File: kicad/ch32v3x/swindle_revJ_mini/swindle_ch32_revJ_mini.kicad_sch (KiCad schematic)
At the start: 16 parts, among them J2_DFU1 con2, U1 CH32V303RCT6, Y1 8Mhz

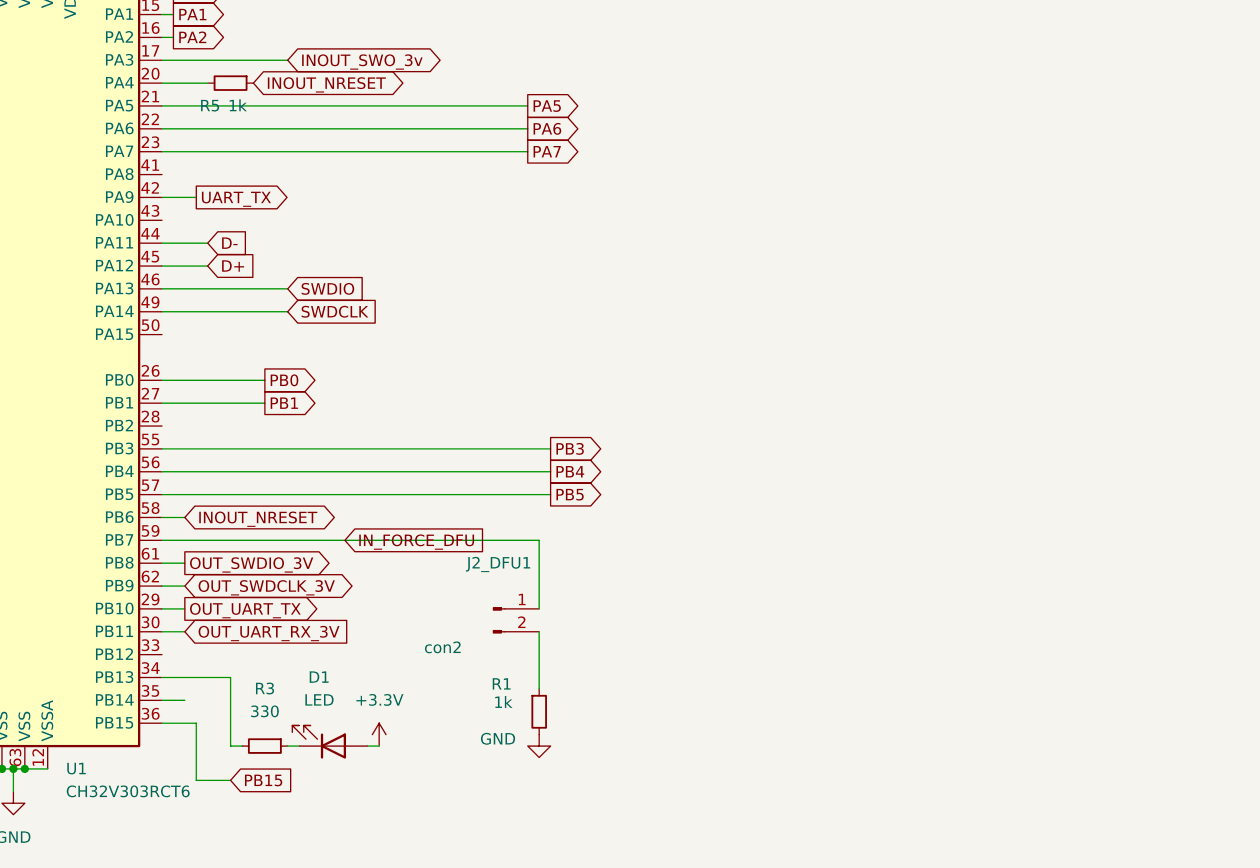
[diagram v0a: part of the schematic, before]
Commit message: add a WS2812b to the mini version, mini version for CH32,GD32 and RP2xxx
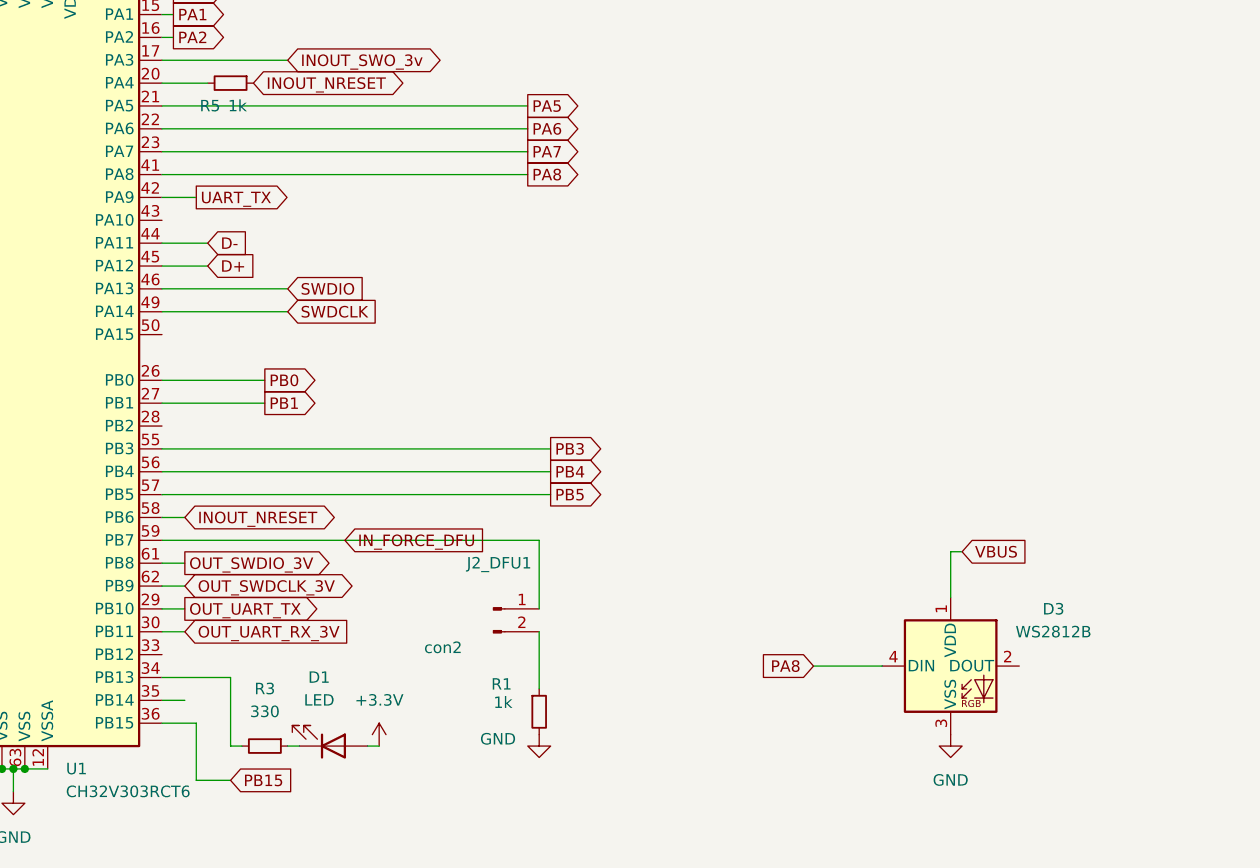
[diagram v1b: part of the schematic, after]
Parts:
- added D3: WS2812B, LED_SMD:LED_WS2812B_PLCC4_5.0x5.0mm_P3.2mm, symbol LED:WS2812B
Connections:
- net GND: now also D3.3 (VSS)
- net PA8: now reaches U1.41 (PA8)
- net PA8: now also D3.4 (DIN)
- new net VBUS: D3.1 (VDD)
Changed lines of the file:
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@@
 	(wire
 		(pts
+			(xy 175.26 129.54) (xy 173.99 129.54)
+		)
+		(stroke
+			(width 0)
+			(type default)
+		)
+	)
+	(wire
+		(pts
 			(xy 38.1 58.42) (xy 38.1 59.69)
 		)
@@
 	(wire
 		(pts
+			(xy 86.36 87.63) (xy 127 87.63)
+		)
+		(stroke
+			(width 0)
+			(type default)
+		)
+	)
+	(wire
+		(pts
 			(xy 86.36 95.25) (xy 91.44 95.25)
 		)
@@
 	(wire
 		(pts
+			(xy 158.75 142.24) (xy 166.37 142.24)
+		)
+		(stroke
+			(width 0)
+			(type default)
+		)
+	)
+	(wire
+		(pts
 			(xy 38.1 43.18) (xy 38.1 44.45)
 		)
@@
 	(wire
 		(pts
+			(xy 173.99 129.54) (xy 173.99 134.62)
+		)
+		(stroke
+			(width 0)
+			(type default)
+		)
+	)
+	(wire
+		(pts
 			(xy 86.36 102.87) (xy 100.33 102.87)
 		)
@@
 		)
 	)
+	(global_label "PA8"
+		(shape input)
+		(at 158.75 142.24 180)
+		(fields_autoplaced yes)
+		(effects
+			(font
+				(size 1.27 1.27)
+			)
+			(justify right)
+		)
+		(property "Intersheetrefs" "${INTERSHEET_REFS}"
+			(at 152.1967 142.24 0)
+			(effects
+				(font
+					(size 1.27 1.27)
+				)
+				(justify right)
+				(hide yes)
+			)
+		)
+	)
 	(global_label "PB1"
 		(shape output)
@@
 		)
 	)
+	(global_label "PA8"
+		(shape output)
+		(at 127 87.63 0)
+		(fields_autoplaced yes)
+		(effects
+			(font
+				(size 1.27 1.27)
+			)
+			(justify left)
+		)
+		(property "Intersheetrefs" "${INTERSHEET_REFS}"
+			(at 133.5533 87.63 0)
+			(effects
+				(font
+					(size 1.27 1.27)
+				)
+				(justify left)
+				(hide yes)
+			)
+		)
+	)
 	(global_label "OUT_UART_TX"
 		(shape output)
@@
 		)
 	)
+	(global_label "VBUS"
+		(shape input)
+		(at 175.26 129.54 0)
+		(fields_autoplaced yes)
+		(effects
+			(font
+				(size 1.27 1.27)
+			)
+			(justify left)
+		)
+		(property "Intersheetrefs" "${INTERSHEET_REFS}"
+			(at 183.1438 129.54 0)
+			(effects
+				(font
+					(size 1.27 1.27)
+				)
+				(justify left)
+				(hide yes)
+			)
+		)
+	)
 	(global_label "PA6"
 		(shape output)
@@
 	)
 	(symbol
+		(lib_id "LED:WS2812B")
+		(at 173.99 142.24 0)
+		(unit 1)
+		(exclude_from_sim no)
+		(in_bom yes)
+		(on_board yes)
+		(dnp no)
+		(fields_autoplaced yes)
+		(property "Reference" "D3"
+			(at 185.42 135.9214 0)
+			(effects
+				(font
+					(size 1.27 1.27)
+				)
+			)
+		)
+		(property "Value" "WS2812B"
+			(at 185.42 138.4614 0)
+			(effects
+				(font
+					(size 1.27 1.27)
+				)
+			)
+		)
+		(property "Footprint" "LED_SMD:LED_WS2812B_PLCC4_5.0x5.0mm_P3.2mm"
+			(at 175.26 149.86 0)
+			(effects
+				(font
+					(size 1.27 1.27)
+				)
+				(justify left top)
+				(hide yes)
+			)
+		)
+		(property "Datasheet" "https://cdn-shop.adafruit.com/datasheets/WS2812B.pdf"
+			(at 176.53 151.765 0)
+			(effects
+				(font
+					(size 1.27 1.27)
+				)
+				(justify left top)
+				(hide yes)
+			)
+		)
+		(property "Description" "RGB LED with integrated controller"
+			(at 173.99 142.24 0)
+			(effects
+				(font
+					(size 1.27 1.27)
+				)
+				(hide yes)
+			)
+		)
+		(pin "2"
+		)
+		(pin "1"
+		)
+		(pin "4"
+		)
+		(pin "3"
+		)
+		(instances
+			(project "swindle_ch32_revJ_mini"
+				(path "/fbe443d6-6d74-4abc-9dee-16e0160553bc"
+					(reference "D3")
+					(unit 1)
+				)
+			)
+		)
+	)
+	(symbol
 		(lib_id "Device:C_Small")
 		(at 119.38 26.67 0)
@@
 					(unit 1)
 				)
+			)
+		)
+	)
+	(symbol
+		(lib_id "power:GND")
+		(at 173.99 149.86 0)
+		(unit 1)
+		(exclude_from_sim no)
+		(in_bom yes)
+		(on_board yes)
+		(dnp no)
+		(fields_autoplaced yes)
+		(property "Reference" "#PWR037"
+			(at 173.99 156.21 0)
+			(effects
+				(font
+					(size 1.27 1.27)
+				)
+				(hide yes)
+			)
+		)
+		(property "Value" "GND"
+			(at 173.99 154.94 0)
+			(effects
+				(font
+					(size 1.27 1.27)
+				)
+			)
+		)
+		(property "Footprint" ""
+			(at 173.99 149.86 0)
+			(effects
+				(font
+					(size 1.27 1.27)
+				)
+				(hide yes)
+			)
+		)
+		(property "Datasheet" ""
+			(at 173.99 149.86 0)
+			(effects
+				(font
+					(size 1.27 1.27)
+				)
+				(hide yes)
+			)
+		)
+		(property "Description" ""
+			(at 173.99 149.86 0)
+			(effects
+				(font
+					(size 1.27 1.27)
+				)
+				(hide yes)
+			)
+		)
+		(pin "1"
+		)
+		(instances
+			(project "swindle_ch32_revJ_mini"
+				(path "/fbe443d6-6d74-4abc-9dee-16e0160553bc"
+					(reference "#PWR037")
+					(unit 1)
+				)

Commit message: kicad: order to pcbway
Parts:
- added C10: 100n, Resistor_SMD:R_0603_1608Metric, symbol Device:C_Small
- added Q1: DMG2302U, Package_TO_SOT_SMD:SOT-23, symbol Transistor_FET:DMG2302U
- added R8: 330, Resistor_SMD:R_0603_1608Metric, symbol Device:R_Small
- added R9: 1k, Resistor_SMD:R_0603_1608Metric, symbol Device:R_Small
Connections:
- net GND: now also C10.2, Q1.2 (S), R9.2
- net INOUT_NRESET: now also R8.1; no longer U1.58 (PB6)
- net PA8: no longer D3.4 (DIN)
- net PB4: now also D3.4 (DIN)
- net VBUS: now also C10.1
- new net: Q1.3 (D), R8.2
- new net DRIVE_RESET: Q1.1 (G), R9.1, U1.58 (PB6)

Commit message: kicad: rename the mostfet as A2SHB
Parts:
- renumbered Q1 to Q1-A2SHB
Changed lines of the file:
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@@
 		(dnp no)
 		(fields_autoplaced yes)
-		(property "Reference" "Q1"
+		(property "Reference" "Q1-A2SHB"
 			(at 186.69 86.3599 0)
 			(effects
@@
 			(project ""
 				(path "/fbe443d6-6d74-4abc-9dee-16e0160553bc"
-					(reference "Q1")
+					(reference "Q1-A2SHB")
 					(unit 1)
 				)

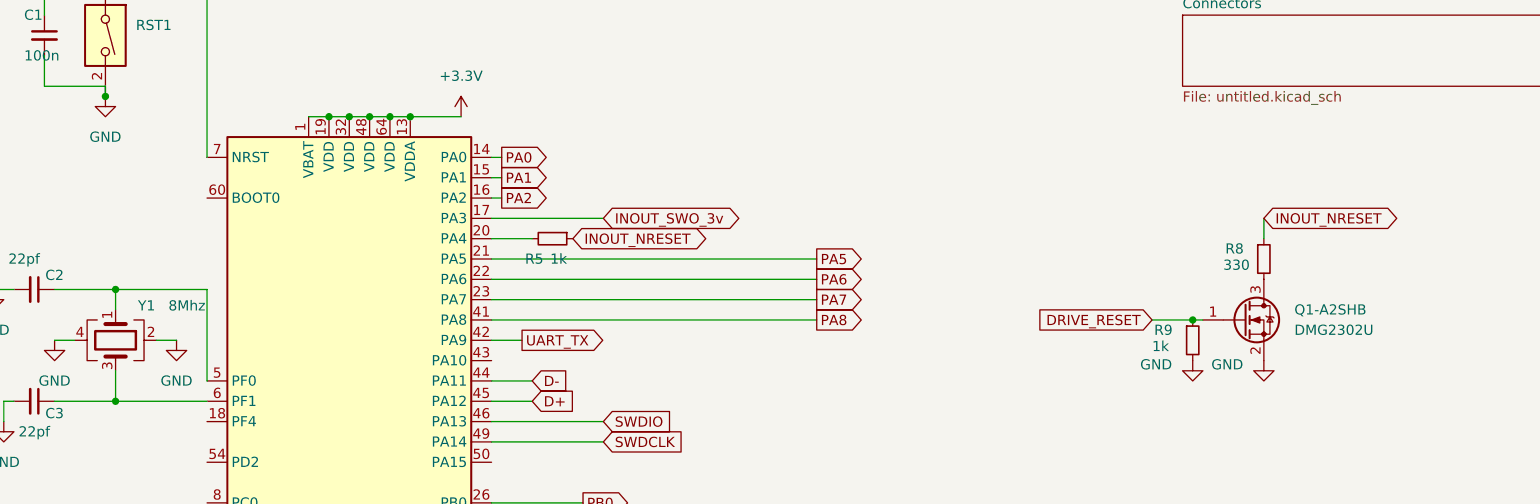
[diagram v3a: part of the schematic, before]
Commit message: kicad/ch32 mini : fix boot0
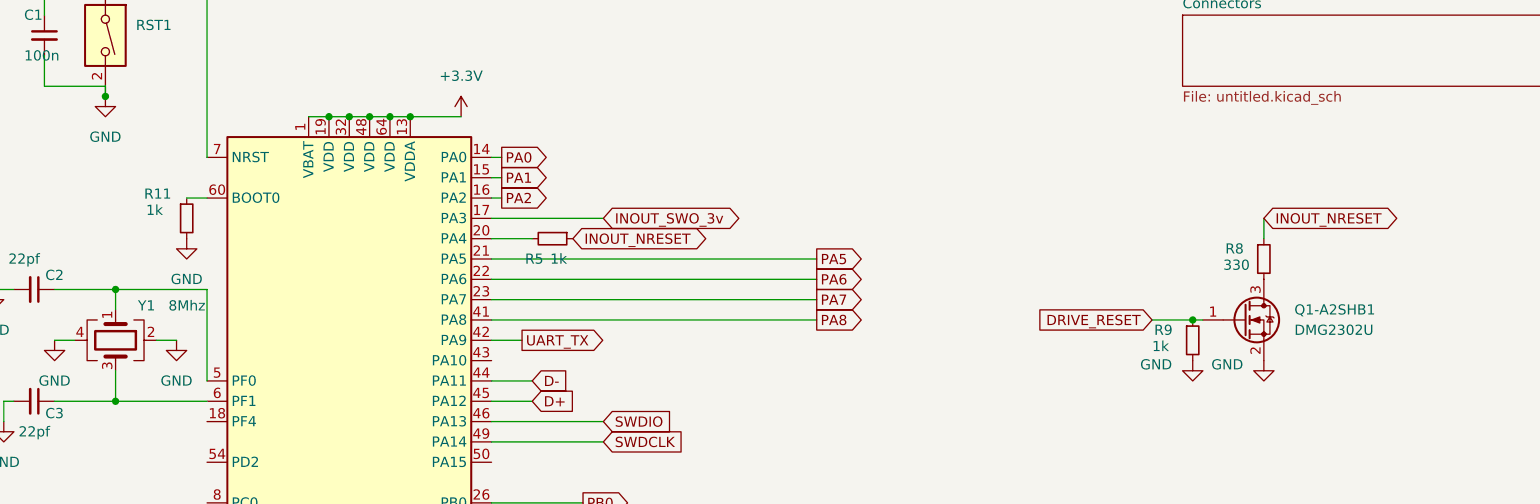
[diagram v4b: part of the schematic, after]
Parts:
- added R11: 1k, Resistor_SMD:R_0603_1608Metric, symbol Device:R_Small
- renumbered Q1-A2SHB to Q1-A2SHB1
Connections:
- net GND: now also R11.2
- net at U1.60 (BOOT0): now also R11.1
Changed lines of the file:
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@@
+	(wire
+		(pts
+			(xy 48.26 72.39) (xy 50.8 72.39)
+		)
+		(stroke
+			(width 0)
+			(type default)
+		)
+	)
 	(wire
 		(pts
@@
 				(justify left)
 				(hide yes)
+			)
+		)
+	)
+	(symbol
+		(lib_id "Device:R_Small")
+		(at 48.26 74.93 0)
+		(unit 1)
+		(exclude_from_sim no)
+		(in_bom yes)
+		(on_board yes)
+		(dnp no)
+		(property "Reference" "R11"
+			(at 42.926 71.882 0)
+			(effects
+				(font
+					(size 1.27 1.27)
+				)
+				(justify left)
+			)
+		)
+		(property "Value" "1k"
+			(at 43.18 73.914 0)
+			(effects
+				(font
+					(size 1.27 1.27)
+				)
+				(justify left)
+			)
+		)
+		(property "Footprint" "Resistor_SMD:R_0603_1608Metric"
+			(at 48.26 74.93 0)
+			(effects
+				(font
+					(size 1.27 1.27)
+				)
+				(hide yes)
+			)
+		)
+		(property "Datasheet" "~"
+			(at 48.26 74.93 0)
+			(effects
+				(font
+					(size 1.27 1.27)
+				)
+				(hide yes)
+			)
+		)
+		(property "Description" ""
+			(at 48.26 74.93 0)
+			(effects
+				(font
+					(size 1.27 1.27)
+				)
+				(hide yes)
+			)
+		)
+		(pin "1"
+		)
+		(pin "2"
+		)
+		(instances
+			(project "swindle_ch32_revJ_mini"
+				(path "/fbe443d6-6d74-4abc-9dee-16e0160553bc"
+					(reference "R11")
+					(unit 1)
+				)
 			)
 		)
@@
 		(dnp no)
 		(fields_autoplaced yes)
-		(property "Reference" "Q1-A2SHB"
+		(property "Reference" "Q1-A2SHB1"
 			(at 186.69 86.3599 0)
 			(effects
@@
 			(project ""
 				(path "/fbe443d6-6d74-4abc-9dee-16e0160553bc"
-					(reference "Q1-A2SHB")
+					(reference "Q1-A2SHB1")
 					(unit 1)
 				)
@@
 					(unit 1)
 				)
+			)
+		)
+	)
+	(symbol
+		(lib_id "power:GND")
+		(at 48.26 77.47 0)
+		(unit 1)
+		(exclude_from_sim no)
+		(in_bom yes)
+		(on_board yes)
+		(dnp no)
+		(fields_autoplaced yes)
+		(property "Reference" "#PWR024"
+			(at 48.26 83.82 0)
+			(effects
+				(font
+					(size 1.27 1.27)
+				)
+				(hide yes)
+			)
+		)
+		(property "Value" "GND"
+			(at 48.26 82.55 0)
+			(effects
+				(font
+					(size 1.27 1.27)
+				)
+			)
+		)
+		(property "Footprint" ""
+			(at 48.26 77.47 0)
+			(effects
+				(font
+					(size 1.27 1.27)
+				)
+				(hide yes)
+			)
+		)
+		(property "Datasheet" ""
+			(at 48.26 77.47 0)
+			(effects
+				(font
+					(size 1.27 1.27)
+				)
+				(hide yes)
+			)
+		)
+		(property "Description" ""
+			(at 48.26 77.47 0)
+			(effects
+				(font
+					(size 1.27 1.27)
+				)
+				(hide yes)
+			)
+		)
+		(pin "1"
+		)
+		(instances
+			(project "swindle_ch32_revJ_mini"
+				(path "/fbe443d6-6d74-4abc-9dee-16e0160553bc"
+					(reference "#PWR024")
+					(unit 1)
+				)
